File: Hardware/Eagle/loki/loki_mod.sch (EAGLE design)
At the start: 38 parts

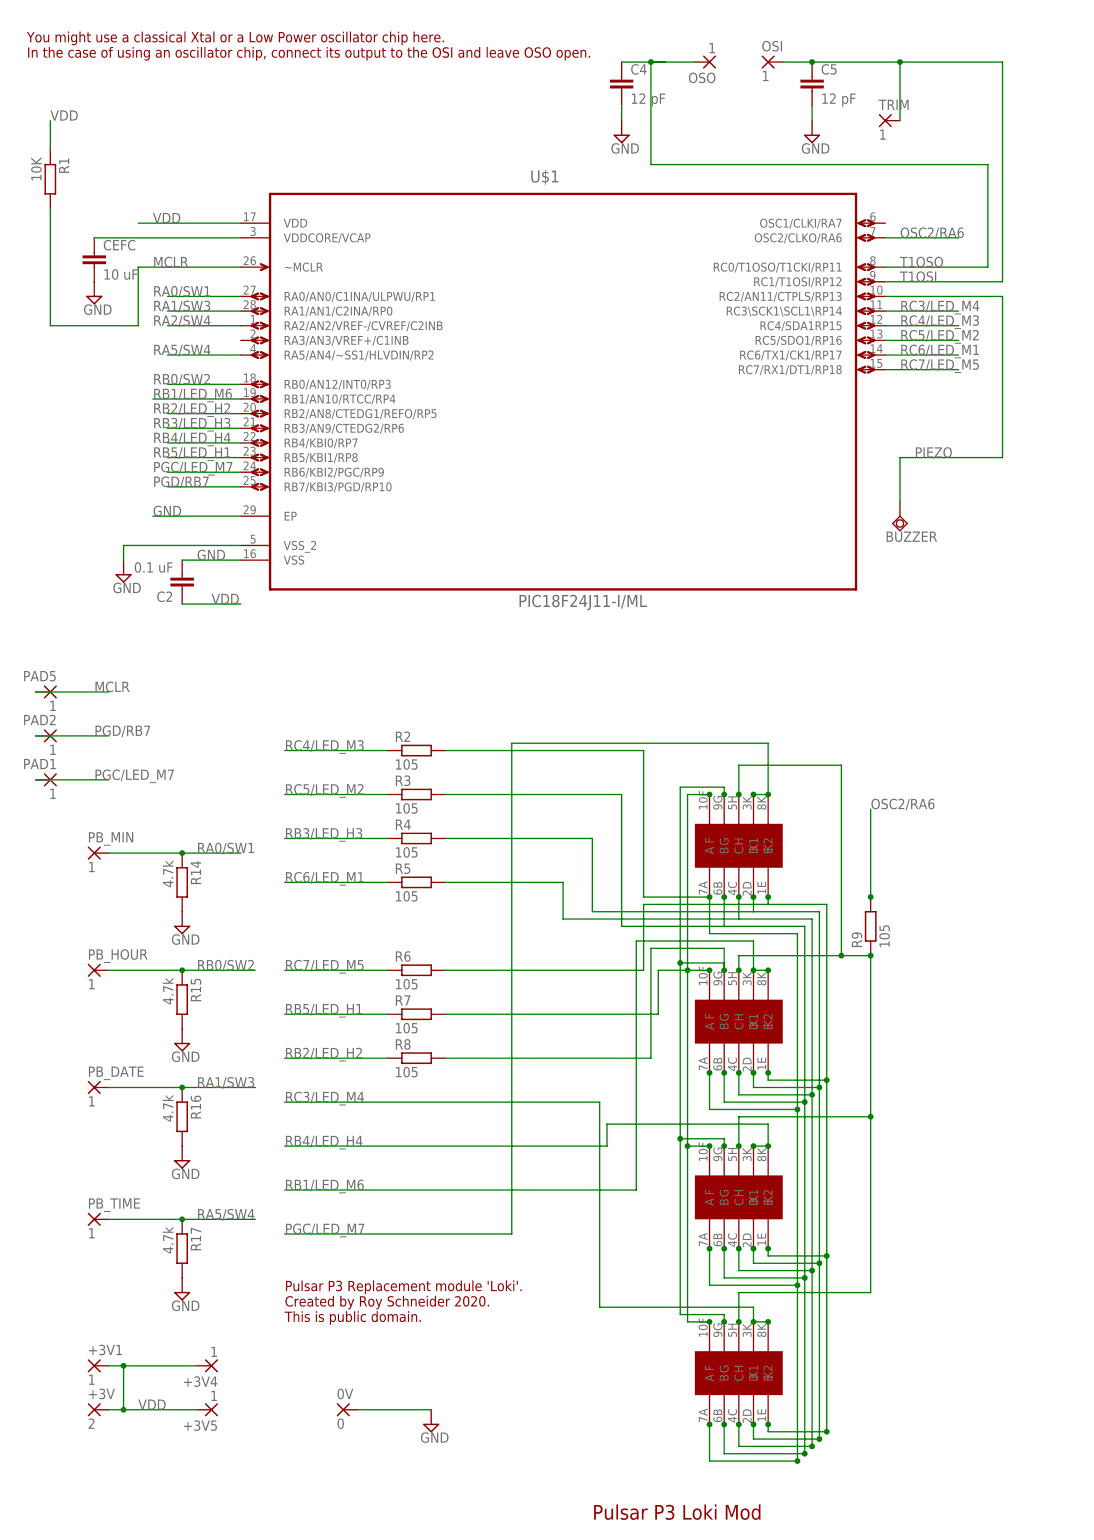
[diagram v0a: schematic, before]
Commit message: Fixed some DRC issues.
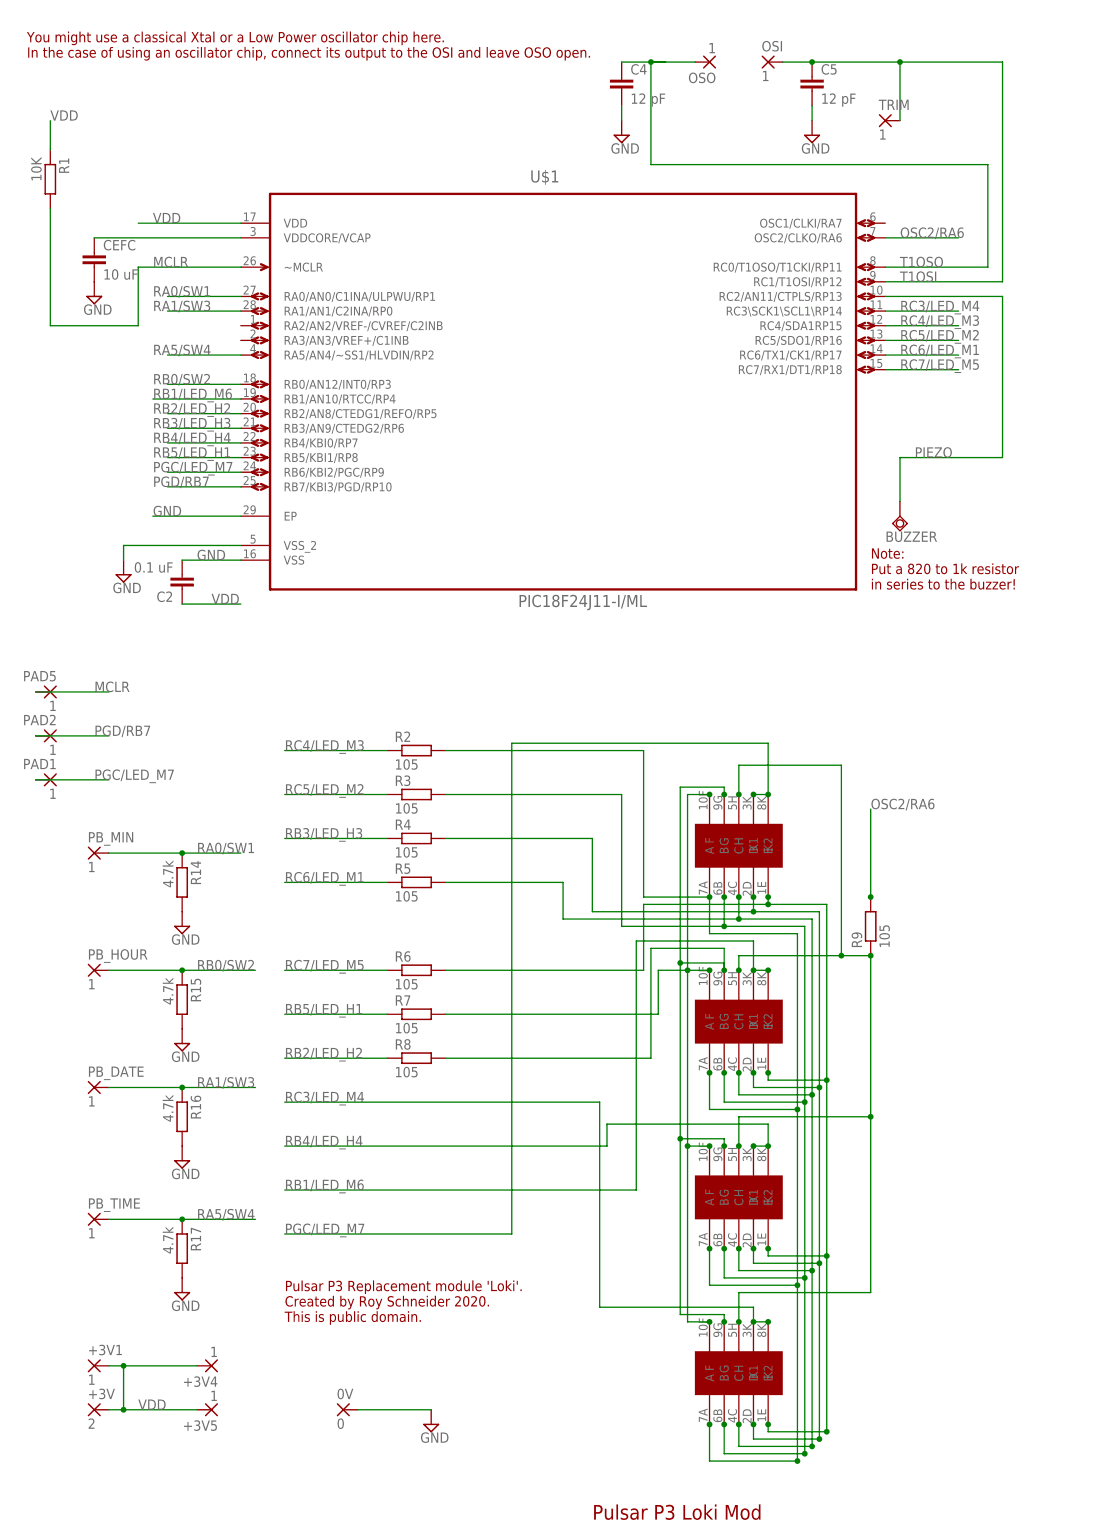
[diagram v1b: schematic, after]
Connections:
- removed net RA2/SW4: U$1.RA2/AN2/VREF-/CVREF/C2INB
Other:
- note added: "Note: Put a 820 to 1k resistor in series to the buzzer!"
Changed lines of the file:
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@@
 This is public domain.</text>
 <text x="-22.86" y="-110.49" size="2.54" layer="94" font="vector">Pulsar P3 Loki Mod</text>
+<text x="25.4" y="50.8" size="1.778" layer="94">Note:
+Put a 820 to 1k resistor
+in series to the buzzer!</text>
 </plain>
 <instances>
@@
 </segment>
 </net>
-<net name="RA2/SW4" class="0">
-<segment>
-<pinref part="U$1" gate="A" pin="RA2/AN2/VREF-/CVREF/C2INB"/>
-<wire x1="-83.82" y1="96.52" x2="-96.52" y2="96.52" width="0.1524" layer="91"/>
-<label x="-99.06" y="96.52" size="1.778" layer="95"/>
-</segment>
-</net>
 <net name="VDDCORE/VCAP" class="0">
 <segment>
@@
 <junction x="0" y="-63.5"/>
 <junction x="0" y="-93.98"/>
+<junction x="0" y="-7.62"/>
 </segment>
 </net>
@@
 <junction x="2.54" y="-63.5"/>
 <junction x="2.54" y="-93.98"/>
+<junction x="2.54" y="-6.35"/>
 </segment>
 </net>
@@
 <junction x="5.08" y="-63.5"/>
 <junction x="5.08" y="-93.98"/>
+<junction x="5.08" y="-5.08"/>
 </segment>
 </net>
@@
 <junction x="7.62" y="-63.5"/>
 <junction x="7.62" y="-93.98"/>
-</segment>
-</net>
+<junction x="7.62" y="-3.81"/>
+</segment>
+</net>

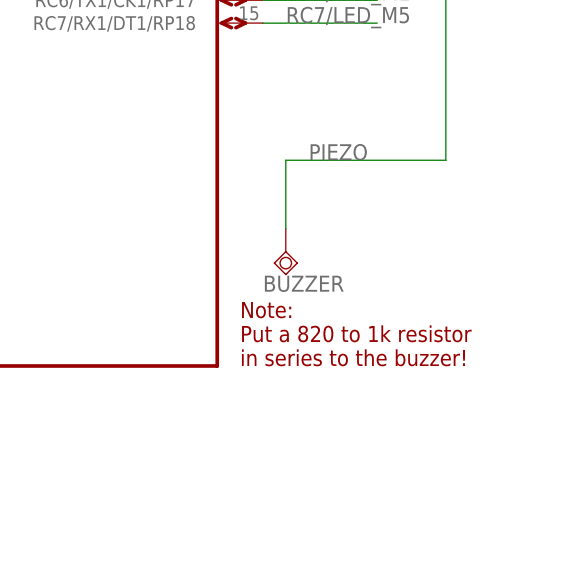
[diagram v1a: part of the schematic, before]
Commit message: Added resitor for piezo.
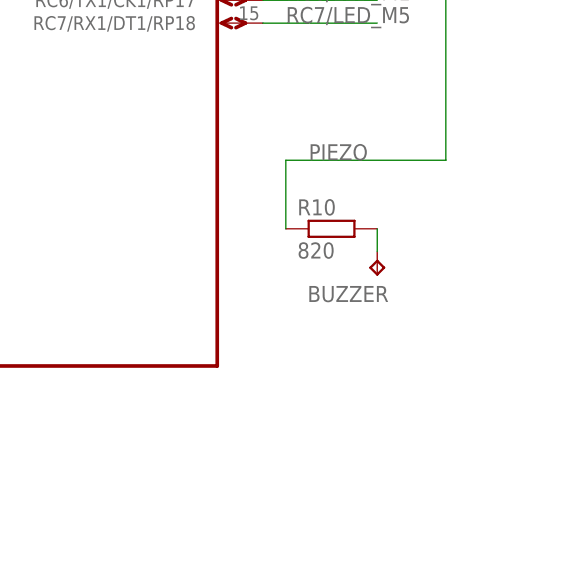
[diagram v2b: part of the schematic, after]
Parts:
- added R10: 820, resistor:R-EU_R0402
- BUZZER: value TPSQTP10SQ -> TPTP06SQ; device testpad:TPSQTP10SQ -> testpad:TPTP06SQ
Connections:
- new net N$1: BUZZER.TP, R10.2
- net PIEZO: now also R10.1; no longer BUZZER.TP
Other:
- note removed: "Note: Put a 820 to 1k resistor in series to the buzzer!"
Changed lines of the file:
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@@
 <part name="1M" library="l104g" deviceset="L104G" device=""/>
 <part name="R9" library="resistor" deviceset="R-EU_" device="R0402" value="105"/>
-<part name="BUZZER" library="testpad" deviceset="TPSQ" device="TP10SQ"/>
+<part name="R10" library="resistor" deviceset="R-EU_" device="R0402" value="820"/>
+<part name="BUZZER" library="testpad" deviceset="TP" device="TP06SQ"/>
 </parts>
 <sheets>
@@
 This is public domain.</text>
 <text x="-22.86" y="-110.49" size="2.54" layer="94" font="vector">Pulsar P3 Loki Mod</text>
-<text x="25.4" y="50.8" size="1.778" layer="94">Note:
-Put a 820 to 1k resistor
-in series to the buzzer!</text>
 </plain>
 <instances>
@@
 <instance part="1M" gate="G$1" x="12.7" y="-63.5" rot="R90"/>
 <instance part="R9" gate="G$1" x="25.4" y="-7.62" rot="R90"/>
-<instance part="BUZZER" gate="G$1" x="30.48" y="63.5"/>
+<instance part="R10" gate="G$1" x="35.56" y="66.04"/>
+<instance part="BUZZER" gate="G$1" x="40.64" y="60.96" rot="R180"/>
 </instances>
 <busses>
@@
 <label x="33.02" y="73.66" size="1.778" layer="95"/>
 <wire x1="30.48" y1="73.66" x2="30.48" y2="66.04" width="0.1524" layer="91"/>
-<pinref part="BUZZER" gate="G$1" pin="TP"/>
+<pinref part="R10" gate="G$1" pin="1"/>
 </segment>
 </net>
@@
 </segment>
 </net>
+<net name="N$1" class="0">
+<segment>
+<pinref part="BUZZER" gate="G$1" pin="TP"/>
+<pinref part="R10" gate="G$1" pin="2"/>
+<wire x1="40.64" y1="63.5" x2="40.64" y2="66.04" width="0.1524" layer="91"/>
+</segment>
+</net>

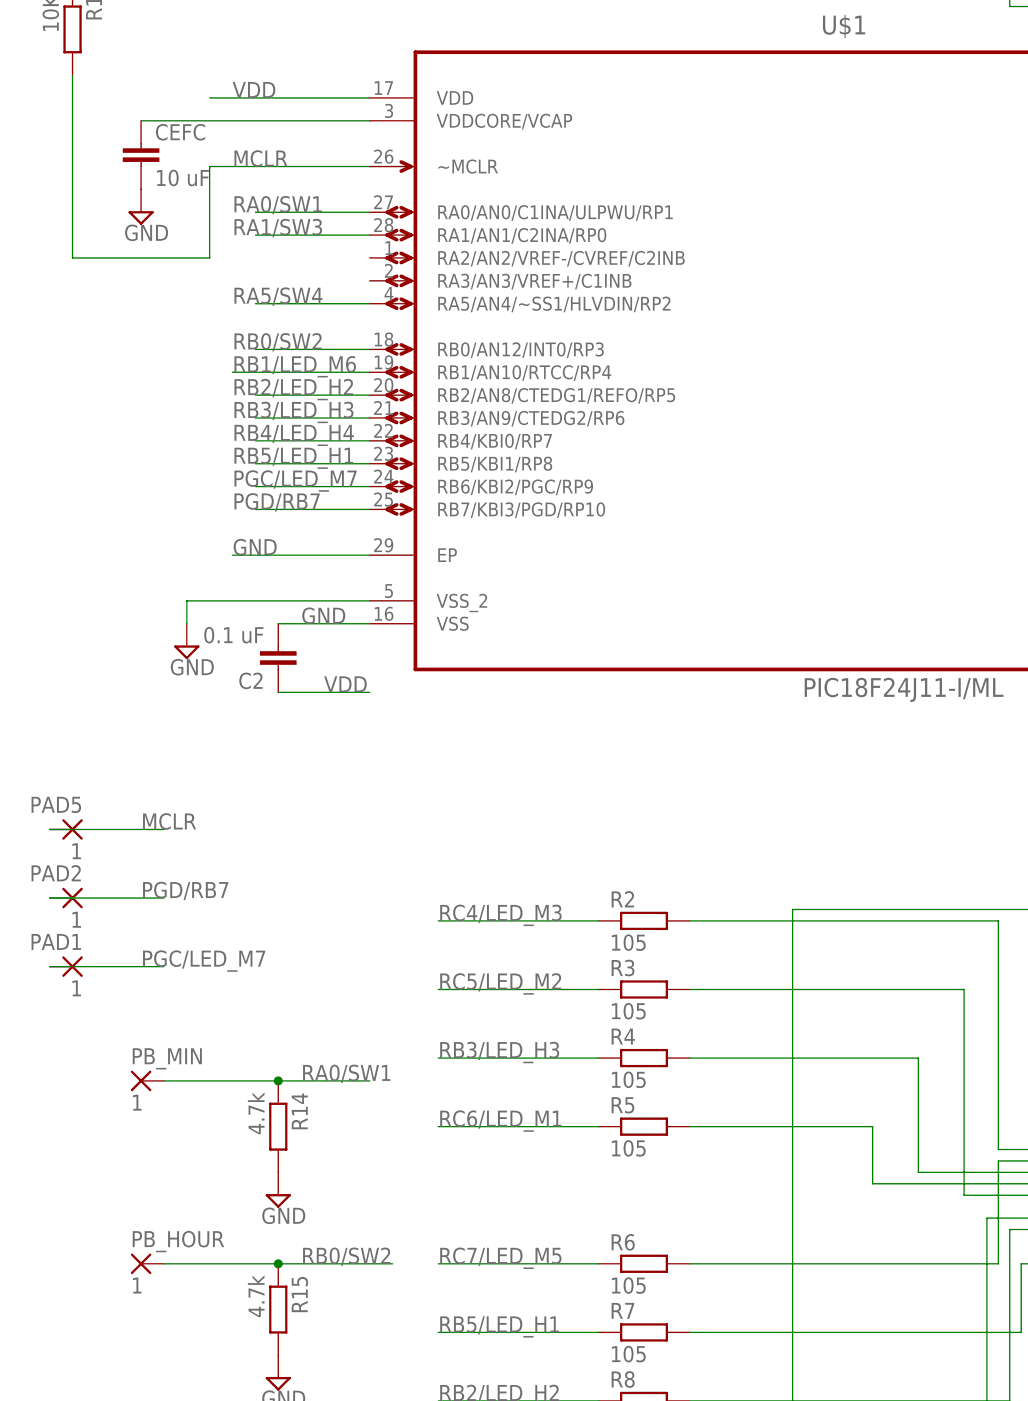
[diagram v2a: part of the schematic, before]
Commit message: Updated resitor values and fine tuned some traces.
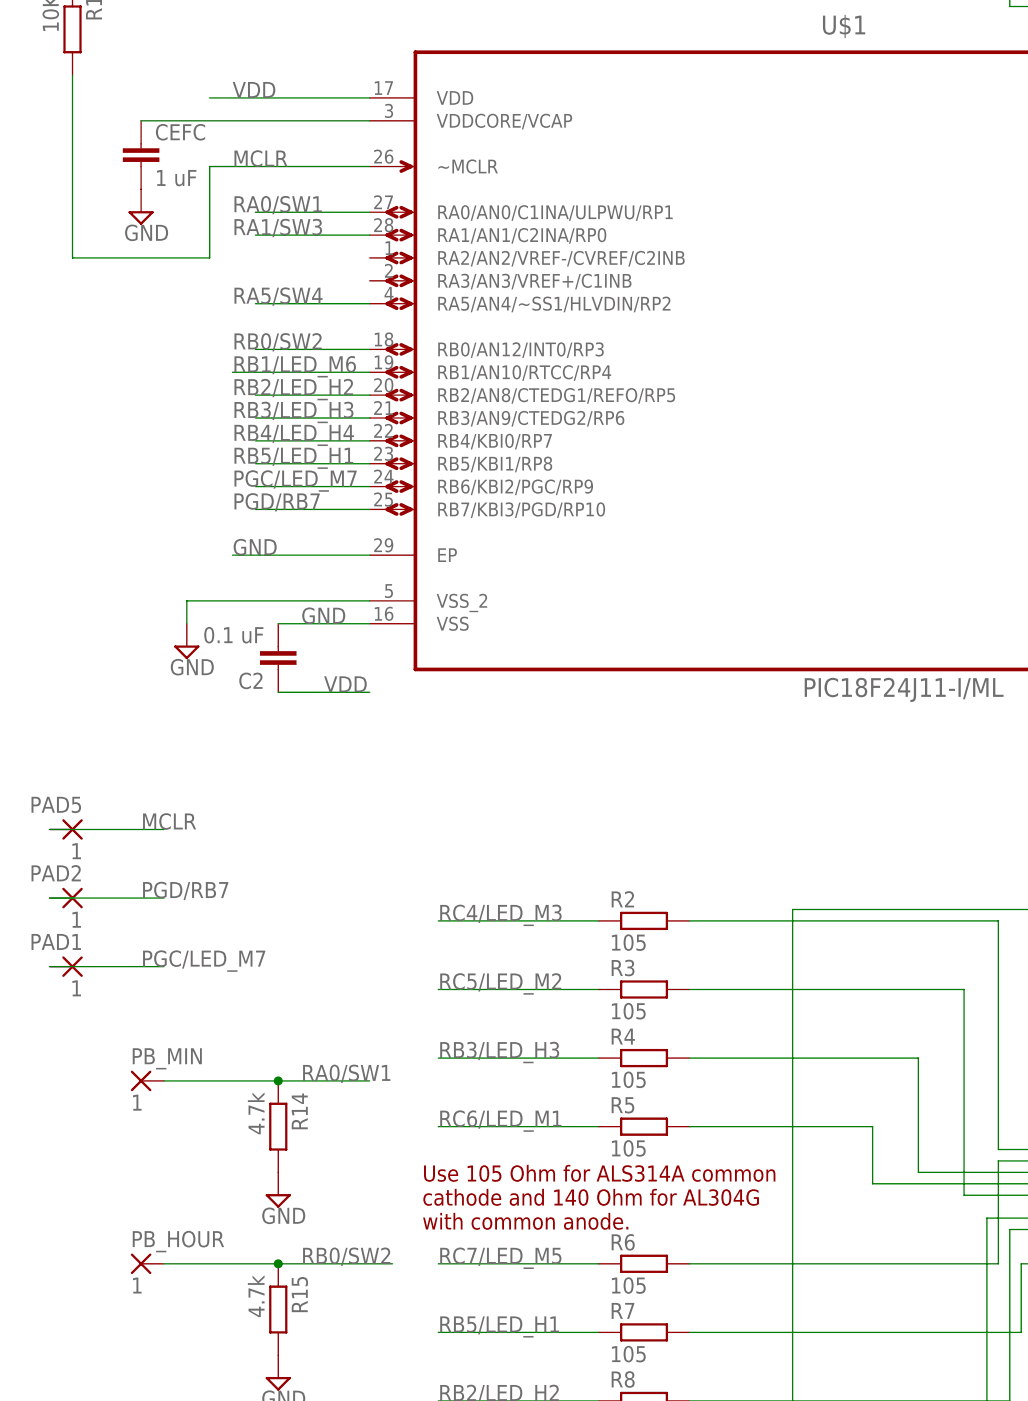
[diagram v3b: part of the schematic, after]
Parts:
- CEFC: value 10 uF -> 1 uF
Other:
- note added: "Use 105 Ohm for ALS314A common cathode and 140 Ohm for AL304G with common anode."
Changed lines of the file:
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@@
 <part name="R1" library="rcl" deviceset="R-EU_" device="R0402" value="10K"/>
 <part name="C2" library="resistor" deviceset="C-EU" device="C0603" value="0.1 uF"/>
-<part name="CEFC" library="resistor" deviceset="C-EU" device="C0603" value="10 uF"/>
+<part name="CEFC" library="resistor" deviceset="C-EU" device="C0603" value="1 uF"/>
 <part name="SUPPLY2" library="supply2" deviceset="GND" device=""/>
 <part name="SUPPLY3" library="supply2" deviceset="GND" device=""/>
@@
 This is public domain.</text>
 <text x="-22.86" y="-110.49" size="2.54" layer="94" font="vector">Pulsar P3 Loki Mod</text>
+<text x="-77.978" y="-11.43" size="1.778" layer="94">Use 105 Ohm for ALS314A common
+cathode and 140 Ohm for AL304G
+with common anode.</text>
 </plain>
 <instances>

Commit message: Reviewed.
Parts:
- CEFC: value 1 uF -> 4.7-10 uF
- R10: value 820 -> 680
- R2, R3, R4, R6, R7, R8, R9: value 105 -> 105/140
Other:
- moved on the sheet: CEFC, R1
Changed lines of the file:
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@@
 <part name="R1" library="rcl" deviceset="R-EU_" device="R0402" value="10K"/>
 <part name="C2" library="resistor" deviceset="C-EU" device="C0603" value="0.1 uF"/>
-<part name="CEFC" library="resistor" deviceset="C-EU" device="C0603" value="1 uF"/>
+<part name="CEFC" library="resistor" deviceset="C-EU" device="C0603" value="4.7-10 uF"/>
 <part name="SUPPLY2" library="supply2" deviceset="GND" device=""/>
 <part name="SUPPLY3" library="supply2" deviceset="GND" device=""/>
-<part name="R2" library="resistor" deviceset="R-EU_" device="R0402" value="105"/>
-<part name="R3" library="resistor" deviceset="R-EU_" device="R0402" value="105"/>
-<part name="R4" library="resistor" deviceset="R-EU_" device="R0402" value="105"/>
+<part name="R2" library="resistor" deviceset="R-EU_" device="R0402" value="105/140"/>
+<part name="R3" library="resistor" deviceset="R-EU_" device="R0402" value="105/140"/>
+<part name="R4" library="resistor" deviceset="R-EU_" device="R0402" value="105/140"/>
 <part name="R5" library="resistor" deviceset="R-EU_" device="R0402" value="105"/>
-<part name="R6" library="resistor" deviceset="R-EU_" device="R0402" value="105"/>
-<part name="R7" library="resistor" deviceset="R-EU_" device="R0402" value="105"/>
-<part name="R8" library="resistor" deviceset="R-EU_" device="R0402" value="105"/>
+<part name="R6" library="resistor" deviceset="R-EU_" device="R0402" value="105/140"/>
+<part name="R7" library="resistor" deviceset="R-EU_" device="R0402" value="105/140"/>
+<part name="R8" library="resistor" deviceset="R-EU_" device="R0402" value="105/140"/>
 <part name="R14" library="resistor" deviceset="R-EU_" device="R0402" value="4.7k"/>
 <part name="R15" library="resistor" deviceset="R-EU_" device="R0402" value="4.7k"/>
@@
 <part name="10M" library="l104g" deviceset="L104G" device=""/>
 <part name="1M" library="l104g" deviceset="L104G" device=""/>
-<part name="R9" library="resistor" deviceset="R-EU_" device="R0402" value="105"/>
-<part name="R10" library="resistor" deviceset="R-EU_" device="R0402" value="820"/>
+<part name="R9" library="resistor" deviceset="R-EU_" device="R0402" value="105/140"/>
+<part name="R10" library="resistor" deviceset="R-EU_" device="R0402" value="680"/>
 <part name="BUZZER" library="testpad" deviceset="TP" device="TP06SQ"/>
 </parts>
@@
 cathode and 140 Ohm for AL304G
 with common anode.</text>
+<text x="39.37" y="-32.258" size="1.778" layer="94" rot="R90">Use 105 Ohm for ALS314A common
+cathode and 140 Ohm for AL304G
+with common anode.</text>
 </plain>
 <instances>
 <instance part="U$1" gate="A" x="-27.94" y="88.9"/>
-<instance part="R1" gate="G$1" x="-116.84" y="121.92" rot="R270"/>
+<instance part="R1" gate="G$1" x="-119.38" y="121.92" rot="R270"/>
 <instance part="C2" gate="G$1" x="-93.98" y="50.8" rot="R180"/>
-<instance part="CEFC" gate="G$1" x="-109.22" y="109.22"/>
-<instance part="SUPPLY2" gate="GND" x="-109.22" y="101.6"/>
+<instance part="CEFC" gate="G$1" x="-114.3" y="109.22"/>
+<instance part="SUPPLY2" gate="GND" x="-114.3" y="101.6"/>
 <instance part="SUPPLY3" gate="GND" x="-104.14" y="53.34"/>
 <instance part="R2" gate="G$1" x="-53.34" y="22.86"/>
@@
 <wire x1="-83.82" y1="106.68" x2="-101.6" y2="106.68" width="0.1524" layer="91"/>
 <wire x1="-101.6" y1="106.68" x2="-101.6" y2="96.52" width="0.1524" layer="91"/>
-<wire x1="-101.6" y1="96.52" x2="-116.84" y2="96.52" width="0.1524" layer="91"/>
+<wire x1="-101.6" y1="96.52" x2="-119.38" y2="96.52" width="0.1524" layer="91"/>
 <label x="-99.06" y="106.68" size="1.778" layer="95"/>
 <pinref part="R1" gate="G$1" pin="2"/>
-<wire x1="-116.84" y1="96.52" x2="-116.84" y2="116.84" width="0.1524" layer="91"/>
+<wire x1="-119.38" y1="96.52" x2="-119.38" y2="116.84" width="0.1524" layer="91"/>
 </segment>
 <segment>
@@
 <segment>
 <pinref part="R1" gate="G$1" pin="1"/>
-<wire x1="-116.84" y1="127" x2="-116.84" y2="132.08" width="0.1524" layer="91"/>
-<label x="-116.84" y="132.08" size="1.778" layer="95"/>
+<wire x1="-119.38" y1="127" x2="-119.38" y2="132.08" width="0.1524" layer="91"/>
+<label x="-119.38" y="132.08" size="1.778" layer="95"/>
 </segment>
 <segment>
@@
 <pinref part="U$1" gate="A" pin="VDDCORE/VCAP"/>
 <pinref part="CEFC" gate="G$1" pin="1"/>
-<wire x1="-83.82" y1="111.76" x2="-109.22" y2="111.76" width="0.1524" layer="91"/>
-</segment>
-</net>
+<wire x1="-83.82" y1="111.76" x2="-114.3" y2="111.76" width="0.1524" layer="91"/>
+</segment>
+</net>
